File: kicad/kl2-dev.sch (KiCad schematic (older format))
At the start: 15 parts, among them CON1 USB-MINI-B, P1 CONN_13, P2 CONN_13, U1 MKL26Z32VFM4, X1 CRYSTAL

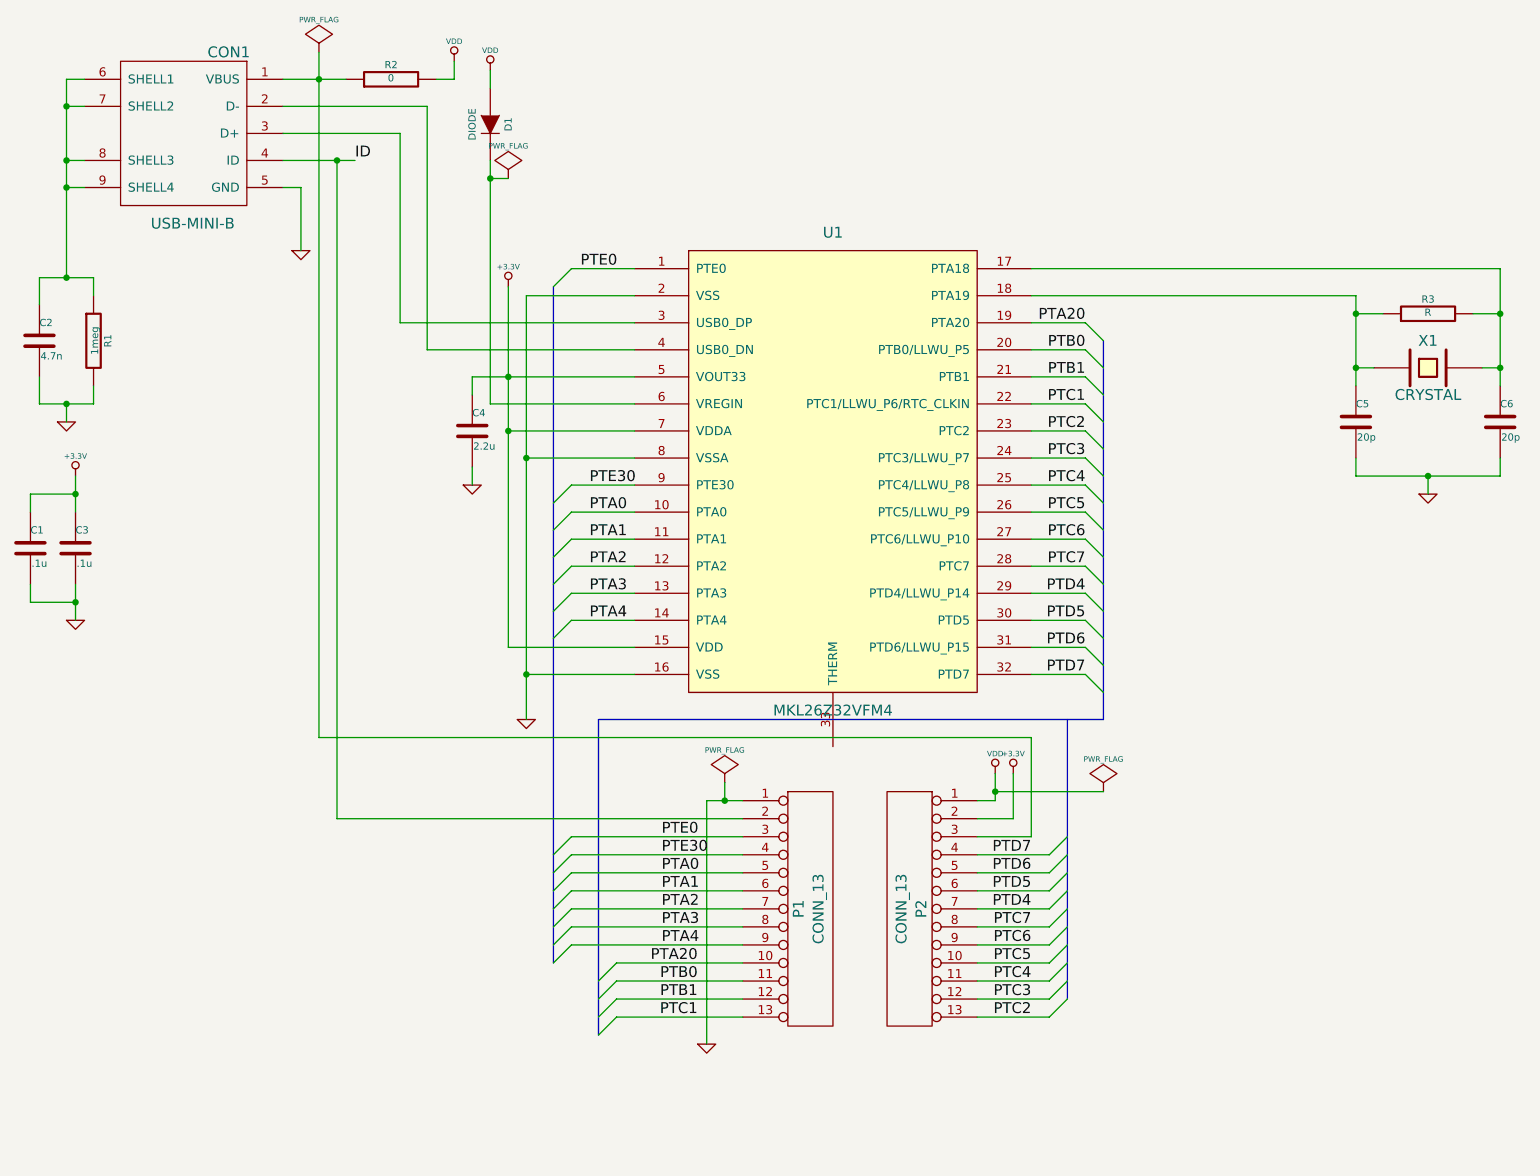
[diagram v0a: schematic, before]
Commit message: Created initial board with demonstration thermal pad
We need pin 33 to be on its own special net because it shouldn't be
connected. We also have not yet routed the flows.
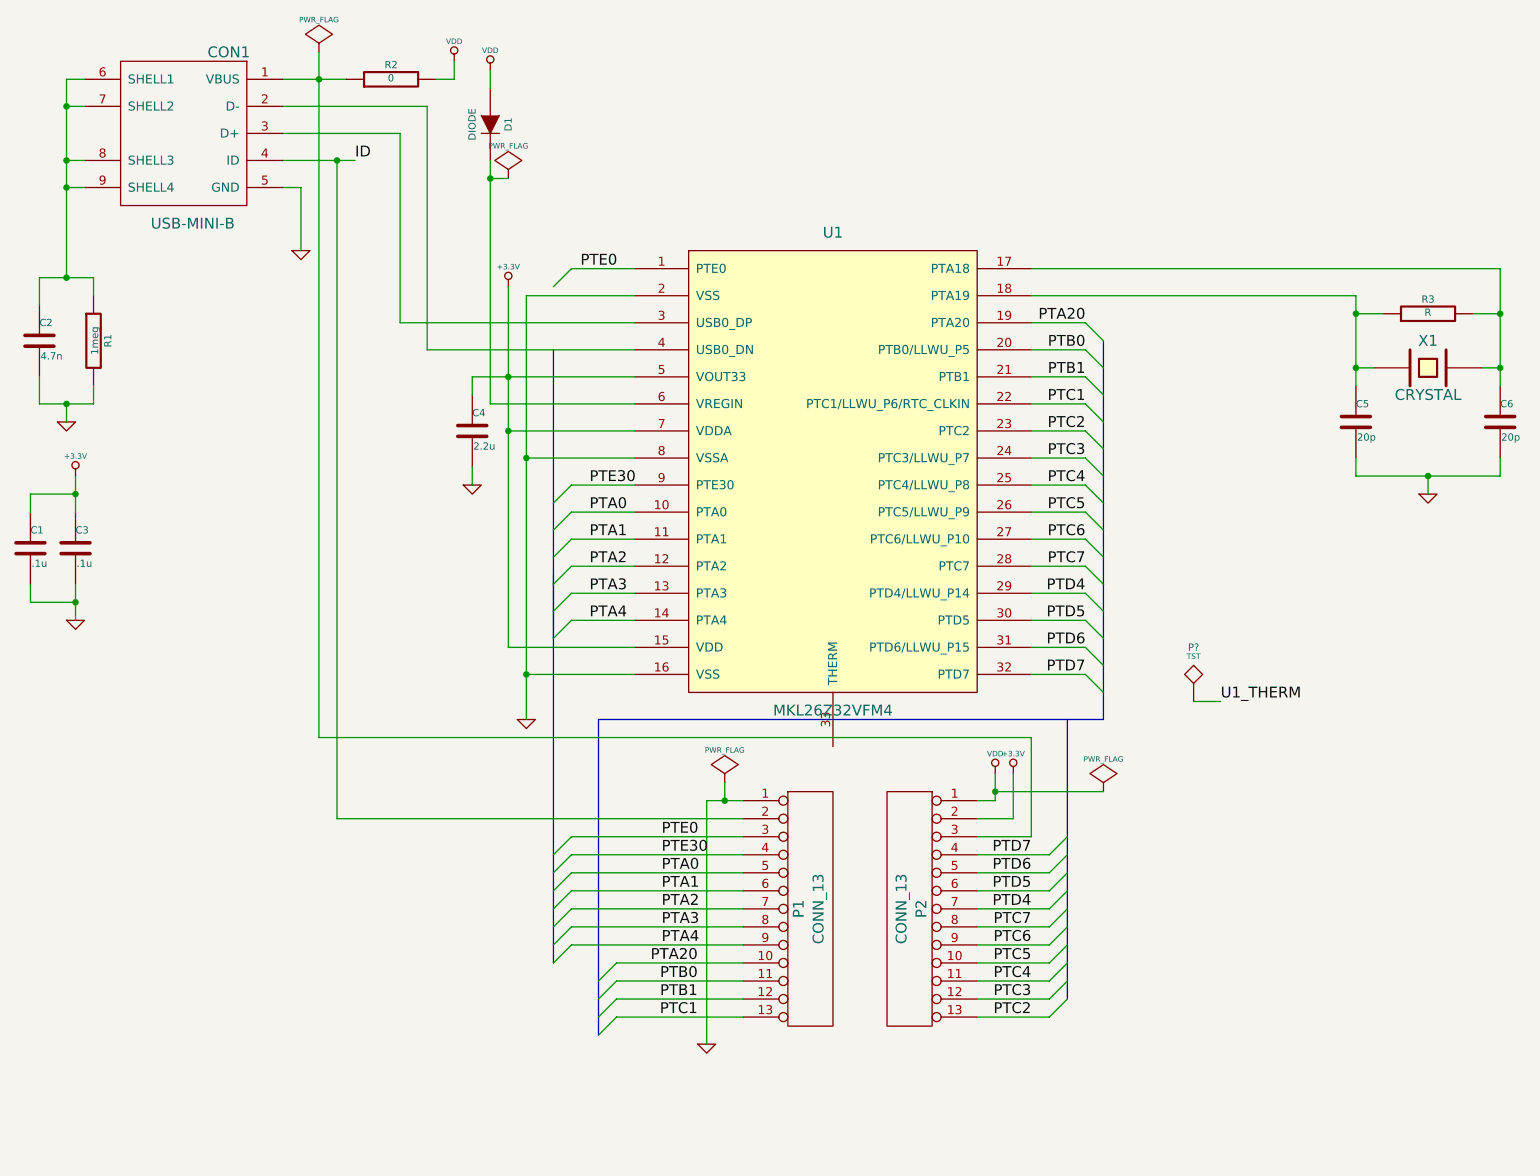
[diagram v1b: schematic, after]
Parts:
- added P?: TST, ~, symbol TST
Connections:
- new net U1_THERM: P?.1

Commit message: Finished routing all but gnd and thermal pad
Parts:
- gave numbers to parts that had none: 1
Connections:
- net U1_THERM: now also U1.33 (THERM)
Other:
- moved on the sheet: P1, P2

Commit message: Fixed a small mistake in a bus on schematic
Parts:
- CON1: Cost (none) -> 0.46; PN (none) -> 609-4616-1-ND
- U1: Cost (none) -> 2.72; PN (none) -> MKL26Z32VFM4-ND
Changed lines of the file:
@@
 F 2 "~" H 1900 1250 60  0000 C CNN
 F 3 "~" H 1900 1250 60  0000 C CNN
+F 4 "609-4616-1-ND" H 1900 1250 60  0001 C CNN "PN"
+F 5 "0.46" H 1900 1250 60  0001 C CNN "Cost"
 	1    1900 1250
 	-1   0    0    -1
@@
 F 2 "~" H 6400 3350 60  0000 C CNN
 F 3 "~" H 6400 3350 60  0000 C CNN
+F 4 "MKL26Z32VFM4-ND" H 5500 3100 60  0001 C CNN "PN"
+F 5 "2.72" H 5500 3100 60  0001 C CNN "Cost"
 	1    5500 3100
 	1    0    0    -1
@@
 	6600 4250 6900 4250
 Wire Bus Line
-	3950 2450 3950 6450
+	3950 2100 3950 6450
 Wire Bus Line
 	7000 2400 7000 4500

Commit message: Added usb resistors and fixed diode packaging
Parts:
- added R? (x2): 33, ~, symbol R
- C2: value 4.7n -> 4700p
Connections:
- net at U1.3 (USB0_DP): now also R?.2; no longer CON1.3 (D+)
- net at U1.4 (USB0_DN): now also R?.2; no longer CON1.2 (D-)
- new net: CON1.2 (D-), R?.1
- new net: CON1.3 (D+), R?.1
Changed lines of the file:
@@
 P 1100 2400
 F 0 "C2" H 1100 2500 40  0000 L CNN
-F 1 "4.7n" H 1106 2315 40  0000 L CNN
+F 1 "4700p" H 1106 2315 40  0000 L CNN
 F 2 "~" H 1138 2250 30  0000 C CNN
 F 3 "~" H 1100 2400 60  0000 C CNN
@@
 	2450 1100 3250 1100
 Wire Wire Line
-	3250 1100 3250 2450
-Wire Wire Line
 	3250 2450 4400 2450
 Wire Wire Line
 	2450 1250 3100 1250
-Wire Wire Line
-	3100 1250 3100 2300
 Wire Wire Line
 	3100 2300 4400 2300
@@
 Wire Wire Line
 	5500 4800 5500 4650
+$Comp
+L R R?
+U 1 1 544BF576
+P 3100 1750
+F 0 "R?" V 3180 1750 40  0000 C CNN
+F 1 "33" V 3107 1751 40  0000 C CNN
+F 2 "~" V 3030 1750 30  0000 C CNN
+F 3 "~" H 3100 1750 30  0000 C CNN
+	1    3100 1750
+	1    0    0    -1
+$EndComp
+$Comp
+L R R?
+U 1 1 544BF585
+P 3250 1750
+F 0 "R?" V 3330 1750 40  0000 C CNN
+F 1 "33" V 3257 1751 40  0000 C CNN
+F 2 "~" V 3180 1750 30  0000 C CNN
+F 3 "~" H 3250 1750 30  0000 C CNN
+	1    3250 1750
+	1    0    0    -1
+$EndComp
+Wire Wire Line
+	3100 1250 3100 1500
+Wire Wire Line
+	3250 1100 3250 1500
+Wire Wire Line
+	3250 2000 3250 2450
+Wire Wire Line
+	3100 2000 3100 2300
 $EndSCHEMATC

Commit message: Final schematic and pcb sent to fabricator
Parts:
- gave numbers to parts that had none: 2
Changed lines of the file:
@@
 $EndComp
 $Comp
-L GND #PWR01
+L GND #PWR4
 U 1 1 54489561
 P 2550 1900
-F 0 "#PWR01" H 2550 1900 30  0001 C CNN
+F 0 "#PWR4" H 2550 1900 30  0001 C CNN
 F 1 "GND" H 2550 1830 30  0001 C CNN
 F 2 "" H 2550 1900 60  0000 C CNN
@@
 $EndComp
 $Comp
-L GND #PWR02
+L GND #PWR1
 U 1 1 54489570
 P 1250 2850
-F 0 "#PWR02" H 1250 2850 30  0001 C CNN
+F 0 "#PWR1" H 1250 2850 30  0001 C CNN
 F 1 "GND" H 1250 2780 30  0001 C CNN
 F 2 "" H 1250 2850 60  0000 C CNN
@@
 $EndComp
 $Comp
-L GND #PWR03
+L GND #PWR3
 U 1 1 5448966C
 P 1300 3950
-F 0 "#PWR03" H 1300 3950 30  0001 C CNN
+F 0 "#PWR3" H 1300 3950 30  0001 C CNN
 F 1 "GND" H 1300 3880 30  0001 C CNN
 F 2 "" H 1300 3950 60  0000 C CNN
@@
 $EndComp
 $Comp
-L VDD #PWR04
+L VDD #PWR5
 U 1 1 544897BB
 P 3400 850
-F 0 "#PWR04" H 3400 950 30  0001 C CNN
+F 0 "#PWR5" H 3400 950 30  0001 C CNN
 F 1 "VDD" H 3400 960 30  0000 C CNN
 F 2 "" H 3400 850 60  0000 C CNN
@@
 $EndComp
 $Comp
-L VDD #PWR05
+L VDD #PWR7
 U 1 1 544897FF
 P 3600 900
-F 0 "#PWR05" H 3600 1000 30  0001 C CNN
+F 0 "#PWR7" H 3600 1000 30  0001 C CNN
 F 1 "VDD" H 3600 1010 30  0000 C CNN
 F 2 "" H 3600 900 60  0000 C CNN
@@
 $EndComp
 $Comp
-L GND #PWR06
+L GND #PWR9
 U 1 1 5448985E
 P 3800 4500
-F 0 "#PWR06" H 3800 4500 30  0001 C CNN
+F 0 "#PWR9" H 3800 4500 30  0001 C CNN
 F 1 "GND" H 3800 4430 30  0001 C CNN
 F 2 "" H 3800 4500 60  0000 C CNN
@@
 $EndComp
 $Comp
-L +3.3V #PWR07
+L +3.3V #PWR2
 U 1 1 544899BB
 P 1300 3150
-F 0 "#PWR07" H 1300 3110 30  0001 C CNN
+F 0 "#PWR2" H 1300 3110 30  0001 C CNN
 F 1 "+3.3V" H 1300 3260 30  0000 C CNN
 F 2 "" H 1300 3150 60  0000 C CNN
@@
 $EndComp
 $Comp
-L +3.3V #PWR08
+L +3.3V #PWR8
 U 1 1 544899D5
 P 3700 2100
-F 0 "#PWR08" H 3700 2060 30  0001 C CNN
+F 0 "#PWR8" H 3700 2060 30  0001 C CNN
 F 1 "+3.3V" H 3700 2210 30  0000 C CNN
 F 2 "" H 3700 2100 60  0000 C CNN
@@
 $EndComp
 $Comp
-L GND #PWR09
+L GND #PWR6
 U 1 1 54489A60
 P 3500 3200
-F 0 "#PWR09" H 3500 3200 30  0001 C CNN
+F 0 "#PWR6" H 3500 3200 30  0001 C CNN
 F 1 "GND" H 3500 3130 30  0001 C CNN
 F 2 "" H 3500 3200 60  0000 C CNN
@@
 $EndComp
 $Comp
-L GND #PWR010
+L GND #PWR13
 U 1 1 54489C3F
 P 8800 3250
-F 0 "#PWR010" H 8800 3250 30  0001 C CNN
+F 0 "#PWR13" H 8800 3250 30  0001 C CNN
 F 1 "GND" H 8800 3180 30  0001 C CNN
 F 2 "" H 8800 3250 60  0000 C CNN
@@
 	6900 4250 7000 4350
 $Comp
-L VDD #PWR011
+L VDD #PWR11
 U 1 1 5448A577
 P 6400 5400
-F 0 "#PWR011" H 6400 5500 30  0001 C CNN
+F 0 "#PWR11" H 6400 5500 30  0001 C CNN
 F 1 "VDD" H 6400 5510 30  0000 C CNN
 F 2 "" H 6400 5400 60  0000 C CNN
@@
 $EndComp
 $Comp
-L +3.3V #PWR012
+L +3.3V #PWR12
 U 1 1 5448A5E5
 P 6500 5400
-F 0 "#PWR012" H 6500 5360 30  0001 C CNN
+F 0 "#PWR12" H 6500 5360 30  0001 C CNN
 F 1 "+3.3V" H 6500 5510 30  0000 C CNN
 F 2 "" H 6500 5400 60  0000 C CNN
@@
 $EndComp
 $Comp
-L GND #PWR013
+L GND #PWR10
 U 1 1 5448A655
 P 4800 6900
-F 0 "#PWR013" H 4800 6900 30  0001 C CNN
+F 0 "#PWR10" H 4800 6900 30  0001 C CNN
 F 1 "GND" H 4800 6830 30  0001 C CNN
 F 2 "" H 4800 6900 60  0000 C CNN
@@
 	6700 6750 6800 6650
 $Comp
-L PWR_FLAG #FLG014
+L PWR_FLAG #FLG4
 U 1 1 5448ADE2
 P 7000 5500
-F 0 "#FLG014" H 7000 5595 30  0001 C CNN
+F 0 "#FLG4" H 7000 5595 30  0001 C CNN
 F 1 "PWR_FLAG" H 7000 5680 30  0000 C CNN
 F 2 "" H 7000 5500 60  0000 C CNN
@@
 $EndComp
 $Comp
-L PWR_FLAG #FLG015
+L PWR_FLAG #FLG1
 U 1 1 5448AE79
 P 2650 800
-F 0 "#FLG015" H 2650 895 30  0001 C CNN
+F 0 "#FLG1" H 2650 895 30  0001 C CNN
 F 1 "PWR_FLAG" H 2650 980 30  0000 C CNN
 F 2 "" H 2650 800 60  0000 C CNN
@@
 $EndComp
 $Comp
-L PWR_FLAG #FLG016
+L PWR_FLAG #FLG2
 U 1 1 5448AF11
 P 3700 1500
-F 0 "#FLG016" H 3700 1595 30  0001 C CNN
+F 0 "#FLG2" H 3700 1595 30  0001 C CNN
 F 1 "PWR_FLAG" H 3700 1680 30  0000 C CNN
 F 2 "" H 3700 1500 60  0000 C CNN
@@
 $EndComp
 $Comp
-L PWR_FLAG #FLG017
+L PWR_FLAG #FLG3
 U 1 1 5448AFA8
 P 4900 5450
-F 0 "#FLG017" H 4900 5545 30  0001 C CNN
+F 0 "#FLG3" H 4900 5545 30  0001 C CNN
 F 1 "PWR_FLAG" H 4900 5630 30  0000 C CNN
 F 2 "" H 4900 5450 60  0000 C CNN
@@
 	5500 4800 5500 4650
 $Comp
-L R R?
+L R R4
 U 1 1 544BF576
 P 3100 1750
-F 0 "R?" V 3180 1750 40  0000 C CNN
+F 0 "R4" V 3180 1750 40  0000 C CNN
 F 1 "33" V 3107 1751 40  0000 C CNN
 F 2 "~" V 3030 1750 30  0000 C CNN
@@
 $EndComp
 $Comp
-L R R?
+L R R5
 U 1 1 544BF585
 P 3250 1750
-F 0 "R?" V 3330 1750 40  0000 C CNN
+F 0 "R5" V 3330 1750 40  0000 C CNN
 F 1 "33" V 3257 1751 40  0000 C CNN
 F 2 "~" V 3180 1750 30  0000 C CNN
